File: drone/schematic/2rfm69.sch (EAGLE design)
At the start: 15 parts, among them IC1 MEGA8-P, Q1 16MHz, U1 RFM692, U2 RFM692

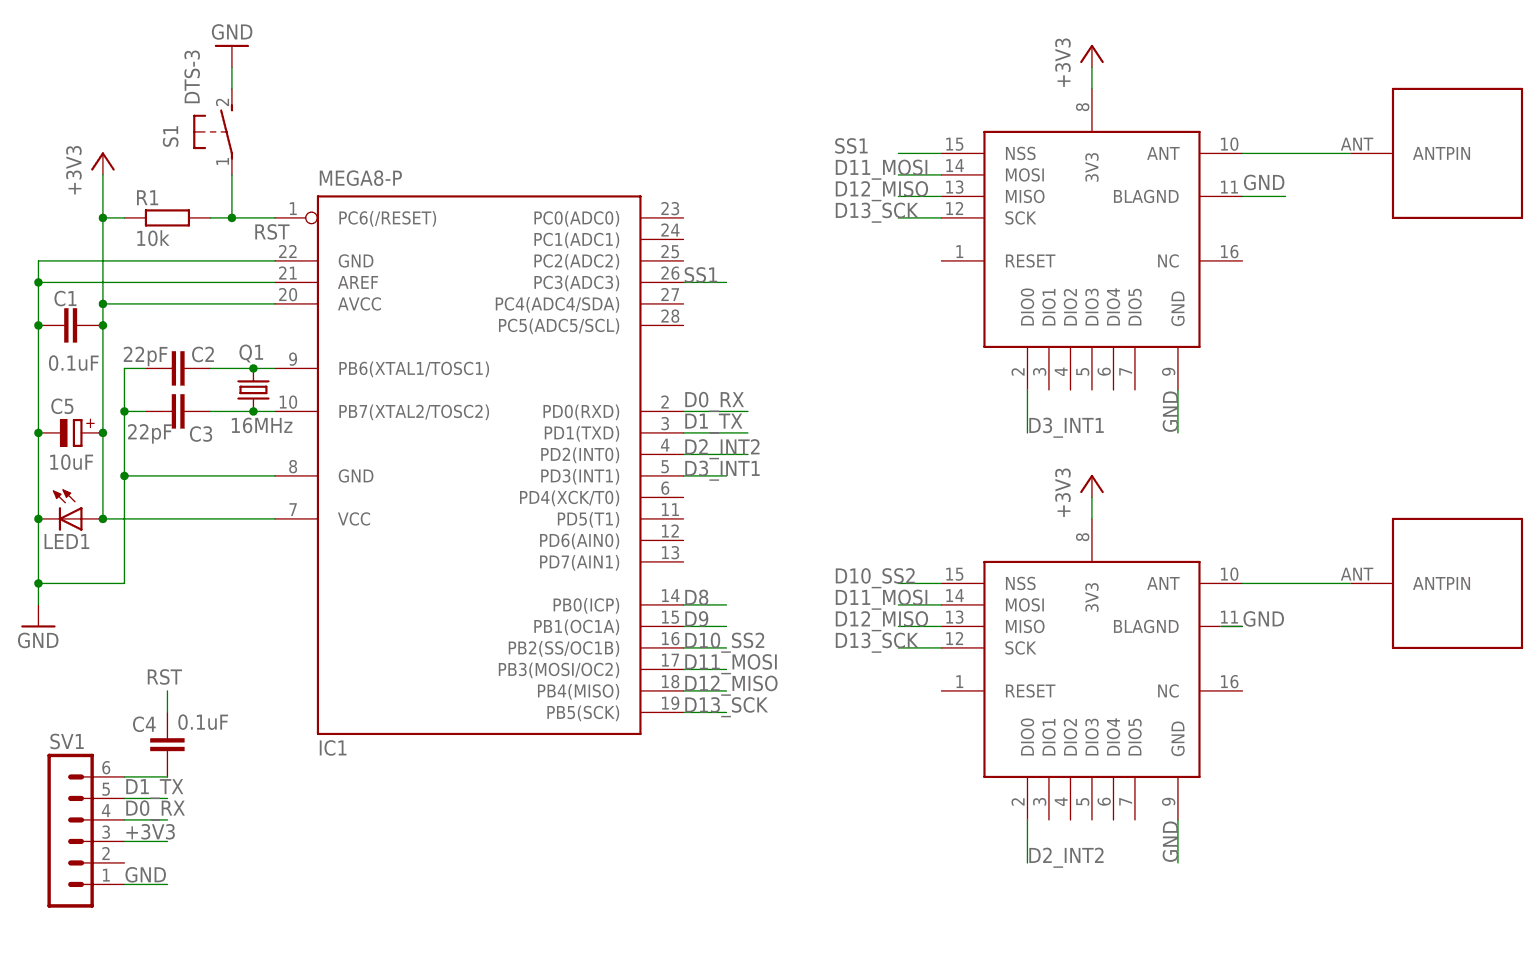
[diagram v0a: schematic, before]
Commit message: test drone DIP schematic complete
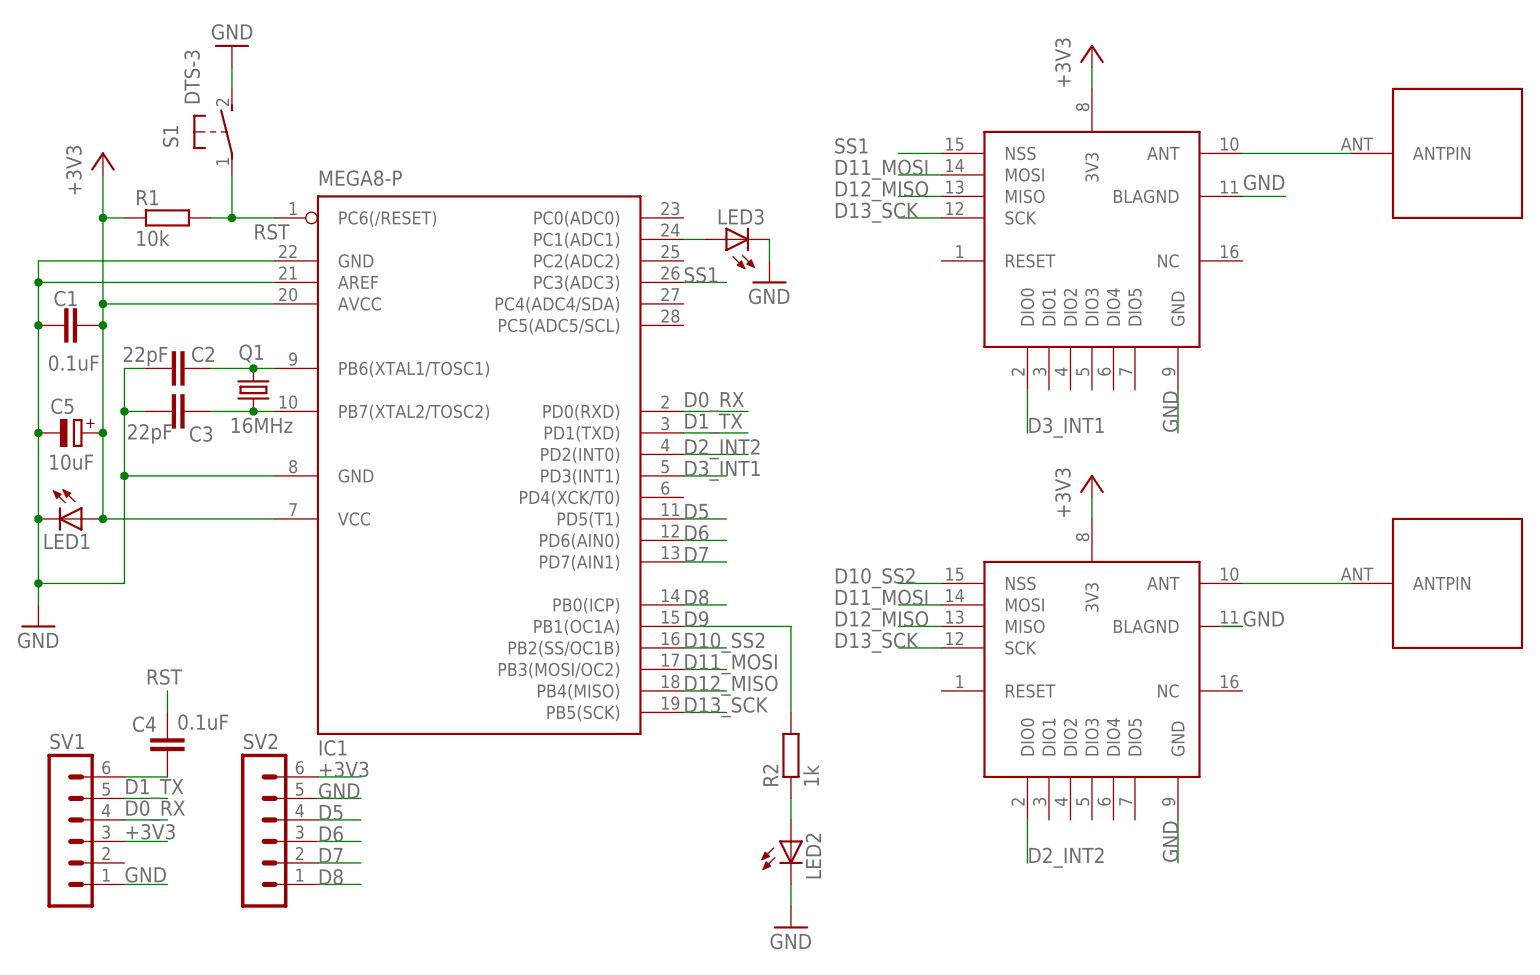
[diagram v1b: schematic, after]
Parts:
- added LED2, LED3: (no value), led:LED3MM
- added R2: 1k, rcl:R-EU_0204/7
- added SV2: (no value), con-lstb:MA06-1
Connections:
- new net D5: IC1.PD5(T1), SV2.4
- new net D6: IC1.PD6(AIN0), SV2.3
- new net D7: IC1.PD7(AIN1), SV2.2
- new net N$6: LED2.A, R2.1
- new net N$7: IC1.PC1(ADC1), LED3.A
- net +3V3: now also SV2.6
- net D8: now also SV2.1
- net D9: now also R2.2
- net GND: now also LED2.C, LED3.C, SV2.5
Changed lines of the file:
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@@
 <setting verticaltext="up"/>
 </settings>
-<grid distance="0.1" unitdist="inch" unit="inch" style="lines" multiple="1" display="yes" altdistance="0.01" altunitdist="inch" altunit="inch"/>
+<grid distance="0.1" unitdist="inch" unit="inch" style="lines" multiple="1" display="no" altdistance="0.01" altunitdist="inch" altunit="inch"/>
 <layers>
 <layer number="1" name="Top" color="4" fill="1" visible="no" active="no"/>
@@
 <part name="U$1" library="rfm69" deviceset="ANT" device=""/>
 <part name="U$2" library="rfm69" deviceset="ANT" device=""/>
+<part name="SV2" library="con-lstb" deviceset="MA06-1" device=""/>
+<part name="LED2" library="led" deviceset="LED" device="3MM"/>
+<part name="R2" library="rcl" deviceset="R-EU_" device="0204/7" value="1k"/>
+<part name="GND3" library="supply1" deviceset="GND" device=""/>
+<part name="LED3" library="led" deviceset="LED" device="3MM"/>
+<part name="GND4" library="supply1" deviceset="GND" device=""/>
 </parts>
 <sheets>
@@
 <instance part="U$1" gate="G$1" x="287.02" y="5.08"/>
 <instance part="U$2" gate="G$1" x="287.02" y="55.88"/>
+<instance part="SV2" gate="1" x="5.08" y="-17.78"/>
+<instance part="LED2" gate="G$1" x="68.58" y="-20.32"/>
+<instance part="R2" gate="G$1" x="68.58" y="-10.16" smashed="yes" rot="R90">
+<attribute name="NAME" x="67.0814" y="-13.97" size="1.778" layer="95" rot="R90"/>
+<attribute name="VALUE" x="71.882" y="-13.97" size="1.778" layer="96" rot="R90"/>
+</instance>
+<instance part="GND3" gate="1" x="68.58" y="-30.48"/>
+<instance part="LED3" gate="G$1" x="60.96" y="50.8" rot="R90"/>
+<instance part="GND4" gate="1" x="66.04" y="45.72"/>
 </instances>
 <busses>
@@
 <pinref part="+3V3" gate="G$1" pin="+3V3"/>
 <wire x1="104.14" y1="68.58" x2="104.14" y2="71.12" width="0.1524" layer="91"/>
+</segment>
+<segment>
+<pinref part="SV2" gate="1" pin="6"/>
+<wire x1="12.7" y1="-12.7" x2="17.78" y2="-12.7" width="0.1524" layer="91"/>
+<label x="12.7" y="-12.7" size="1.778" layer="95"/>
 </segment>
 </net>
@@
 <label x="127" y="58.42" size="1.778" layer="95" rot="R180"/>
 </segment>
+<segment>
+<pinref part="SV2" gate="1" pin="5"/>
+<wire x1="12.7" y1="-15.24" x2="17.78" y2="-15.24" width="0.1524" layer="91"/>
+<label x="12.7" y="-15.24" size="1.778" layer="95"/>
+</segment>
+<segment>
+<pinref part="LED2" gate="G$1" pin="C"/>
+<wire x1="68.58" y1="-25.4" x2="68.58" y2="-27.94" width="0.1524" layer="91"/>
+<pinref part="GND3" gate="1" pin="GND"/>
+</segment>
+<segment>
+<pinref part="LED3" gate="G$1" pin="C"/>
+<pinref part="GND4" gate="1" pin="GND"/>
+<wire x1="66.04" y1="50.8" x2="66.04" y2="48.26" width="0.1524" layer="91"/>
+</segment>
 </net>
 <net name="N$1" class="0">
@@
 <label x="55.88" y="7.62" size="1.778" layer="95"/>
 </segment>
+<segment>
+<pinref part="SV2" gate="1" pin="1"/>
+<wire x1="12.7" y1="-25.4" x2="17.78" y2="-25.4" width="0.1524" layer="91"/>
+<label x="12.7" y="-25.4" size="1.778" layer="95"/>
+</segment>
 </net>
 <net name="D10_SS2" class="0">
@@
 <segment>
 <pinref part="IC1" gate="G$1" pin="PB1(OC1A)"/>
-<wire x1="55.88" y1="5.08" x2="60.96" y2="5.08" width="0.1524" layer="91"/>
 <label x="55.88" y="5.08" size="1.778" layer="95"/>
+<wire x1="55.88" y1="5.08" x2="68.58" y2="5.08" width="0.1524" layer="91"/>
+<wire x1="68.58" y1="5.08" x2="68.58" y2="-5.08" width="0.1524" layer="91"/>
+<pinref part="R2" gate="G$1" pin="2"/>
 </segment>
 </net>
@@
 </segment>
 </net>
+<net name="D7" class="0">
+<segment>
+<pinref part="SV2" gate="1" pin="2"/>
+<wire x1="12.7" y1="-22.86" x2="17.78" y2="-22.86" width="0.1524" layer="91"/>
+<label x="12.7" y="-22.86" size="1.778" layer="95"/>
+</segment>
+<segment>
+<pinref part="IC1" gate="G$1" pin="PD7(AIN1)"/>
+<wire x1="55.88" y1="12.7" x2="60.96" y2="12.7" width="0.1524" layer="91"/>
+<label x="55.88" y="12.7" size="1.778" layer="95"/>
+</segment>
+</net>
+<net name="D6" class="0">
+<segment>
+<pinref part="IC1" gate="G$1" pin="PD6(AIN0)"/>
+<wire x1="55.88" y1="15.24" x2="60.96" y2="15.24" width="0.1524" layer="91"/>
+<label x="55.88" y="15.24" size="1.778" layer="95"/>
+</segment>
+<segment>
+<pinref part="SV2" gate="1" pin="3"/>
+<wire x1="12.7" y1="-20.32" x2="17.78" y2="-20.32" width="0.1524" layer="91"/>
+<label x="12.7" y="-20.32" size="1.778" layer="95"/>
+</segment>
+</net>
+<net name="D5" class="0">
+<segment>
+<pinref part="IC1" gate="G$1" pin="PD5(T1)"/>
+<wire x1="55.88" y1="17.78" x2="60.96" y2="17.78" width="0.1524" layer="91"/>
+<label x="55.88" y="17.78" size="1.778" layer="95"/>
+</segment>
+<segment>
+<pinref part="SV2" gate="1" pin="4"/>
+<wire x1="12.7" y1="-17.78" x2="17.78" y2="-17.78" width="0.1524" layer="91"/>
+<label x="12.7" y="-17.78" size="1.778" layer="95"/>
+</segment>
+</net>
+<net name="N$6" class="0">
+<segment>
+<pinref part="R2" gate="G$1" pin="1"/>
+<pinref part="LED2" gate="G$1" pin="A"/>
+<wire x1="68.58" y1="-15.24" x2="68.58" y2="-17.78" width="0.1524" layer="91"/>
+</segment>
+</net>
+<net name="N$7" class="0">
+<segment>
+<pinref part="IC1" gate="G$1" pin="PC1(ADC1)"/>
+<pinref part="LED3" gate="G$1" pin="A"/>
+<wire x1="55.88" y1="50.8" x2="58.42" y2="50.8" width="0.1524" layer="91"/>
+</segment>
+</net>
